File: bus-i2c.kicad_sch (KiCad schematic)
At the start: 2 parts

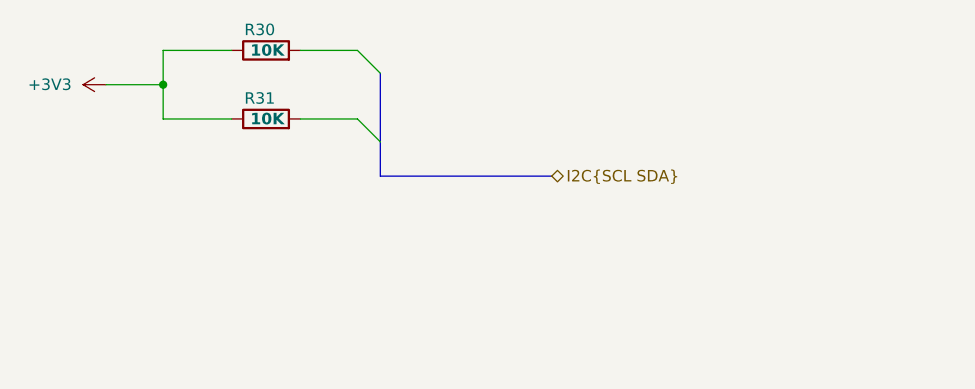
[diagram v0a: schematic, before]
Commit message: Adding testpoints to I2C, SPI, and signals
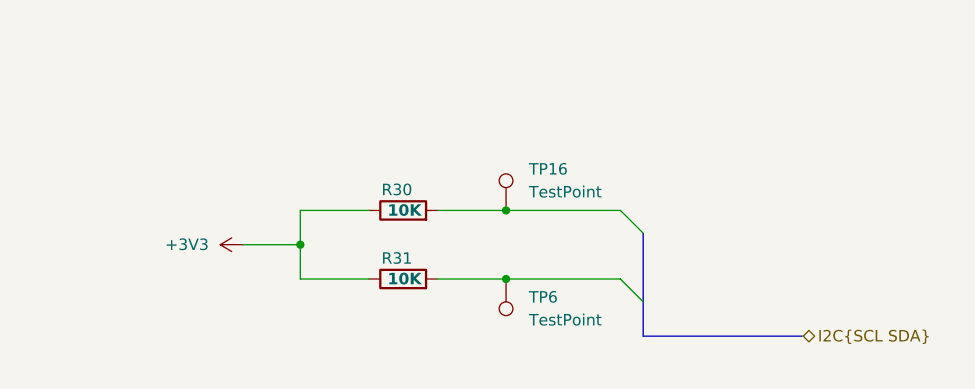
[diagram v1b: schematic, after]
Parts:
- added TP16, TP6: TestPoint, TestPoint:TestPoint_Loop_D2.50mm_Drill1.0mm, symbol Connector:TestPoint
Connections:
- net at R31.2: now also TP6.1
- net at R30.2: now also TP16.1
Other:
- moved on the sheet: R30, R31

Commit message: Fixing lots of ERC errors
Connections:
- net I2C.SDA: now reaches R30.2, TP16.1
- net I2C.SCL: now reaches R31.2, TP6.1
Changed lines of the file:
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@@
+		)
+	)
+	(label "I2C.SCL"
+		(at 138.43 102.87 0)
+		(fields_autoplaced yes)
+		(effects
+			(font
+				(size 1.27 1.27)
+			)
+			(justify left bottom)
+		)
+	)
+	(label "I2C.SDA"
+		(at 138.43 95.25 0)
+		(fields_autoplaced yes)
+		(effects
+			(font
+				(size 1.27 1.27)
+			)
+			(justify left bottom)
 		)
 	)
@@
 		(on_board yes)
 		(dnp no)
-		(fields_autoplaced yes)
 		(property "Reference" "TP16"
-			(at 138.43 90.6779 0)
+			(at 134.62 87.122 0)
 			(effects
 				(font
@@
 		)
 		(property "Value" "TestPoint"
-			(at 138.43 93.2179 0)
+			(at 134.62 89.662 0)
 			(effects
 				(font
@@
 		)
 		(pin "1"
+		)
+		(instances
+			(project "roamer"
+				(path "/1c59de6a-87fe-4223-8898-4b0383164a31/beda7724-0f76-4222-b818-cdbe579d0fe4"
+					(reference "TP16")
+					(unit 1)
+				)
+			)
 		)
 	)
@@
 		(on_board yes)
 		(dnp no)
-		(fields_autoplaced yes)
 		(property "Reference" "TP6"
-			(at 138.43 104.9019 0)
+			(at 135.128 109.22 0)
 			(effects
 				(font
@@
 		)
 		(property "Value" "TestPoint"
-			(at 138.43 107.4419 0)
-			(effects
-				(font
+			(at 135.128 111.76 0)
+			(effects
+				(font

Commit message: Redid board layout. Still have to add bypass caps
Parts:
- removed TP16, TP6: TestPoint, TestPoint:TestPoint_Loop_D2.50mm_Drill1.0mm, symbol Connector:TestPoint
